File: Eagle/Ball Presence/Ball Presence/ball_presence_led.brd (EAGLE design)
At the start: 26.4 x 24.4 mm, 5 parts

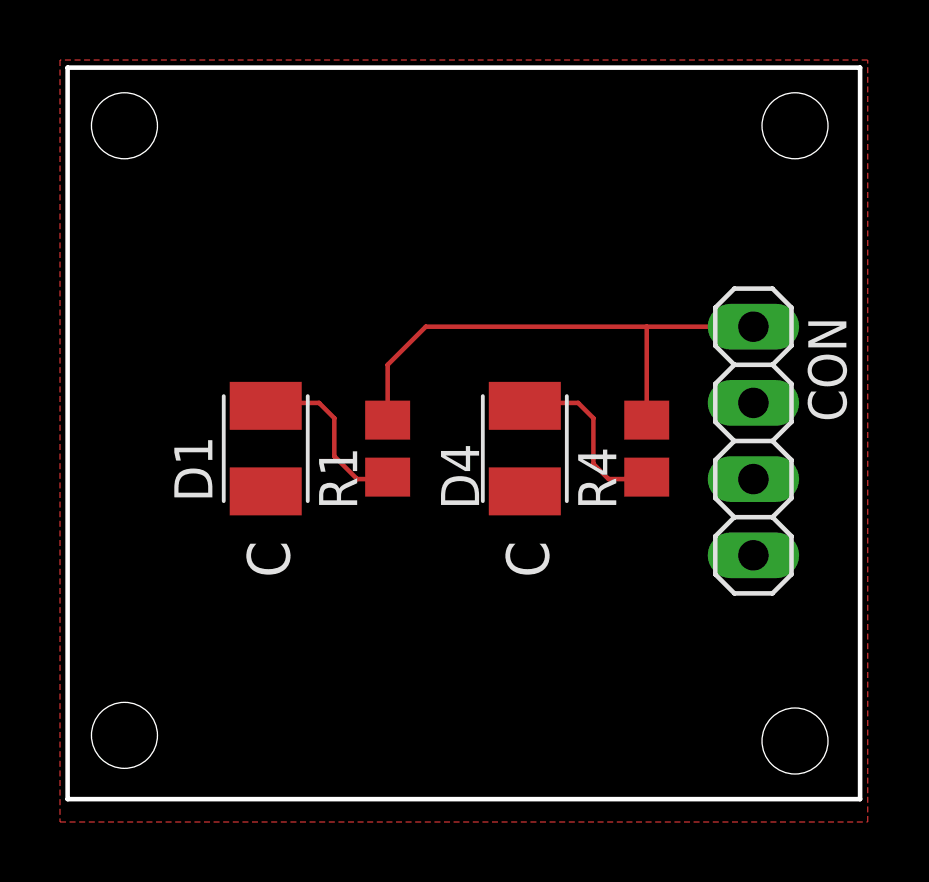
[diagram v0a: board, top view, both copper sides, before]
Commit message: ball presence sensor v1.0
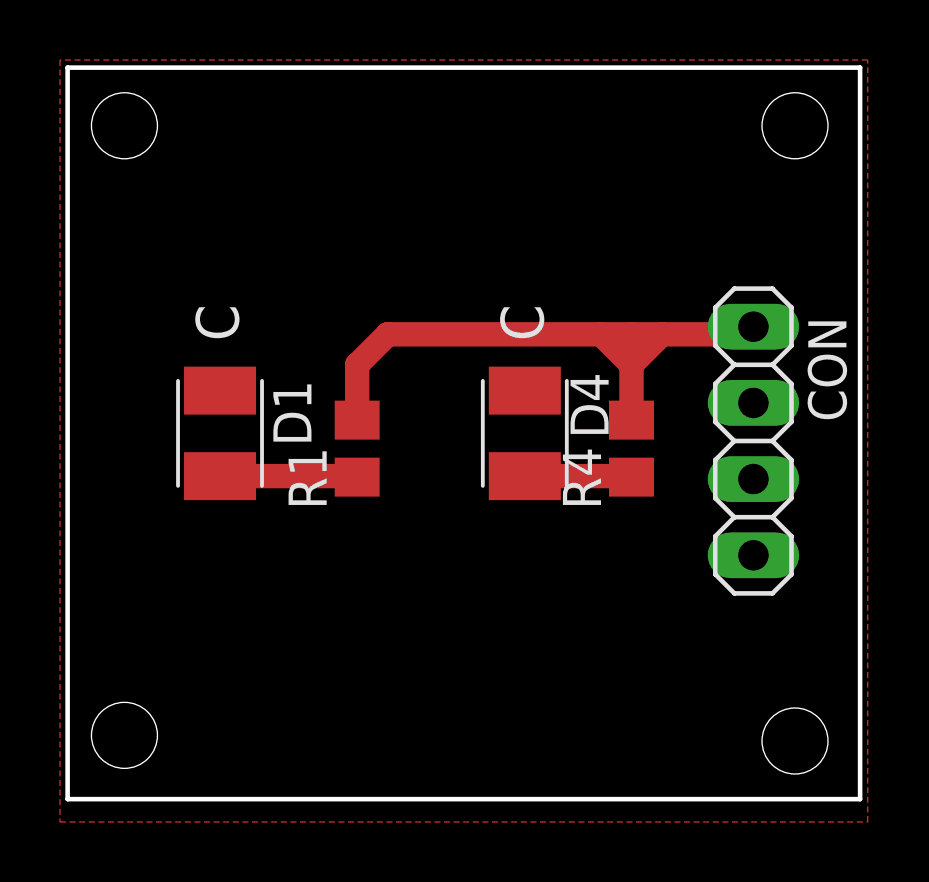
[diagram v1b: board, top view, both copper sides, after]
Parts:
- moved D1 1.61 mm to (6.10, 13.5), turned to 270 degrees
- moved R1 1.02 mm to (10.7, 13.0)
- moved D4 0.51 mm to (16.3, 13.5), turned to 270 degrees
- moved R4 0.51 mm to (19.8, 13.0)
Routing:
- net V+: track 17.7 -> 21.6 mm
- net N$4: track 6.08 -> 3.57 mm
- net N$1: track 5.93 -> 4.68 mm
